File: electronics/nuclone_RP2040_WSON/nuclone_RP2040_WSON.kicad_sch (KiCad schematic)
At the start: 36 parts, among them J1 JTAG_2X05, J2 TYPE-C-31-M-12, J3 nuclone_small_left, J4 nuclone_small_right, SW1 RESET, SW2 Bootloader, U1 MCP1702-MB, U2 TPESD0504C6

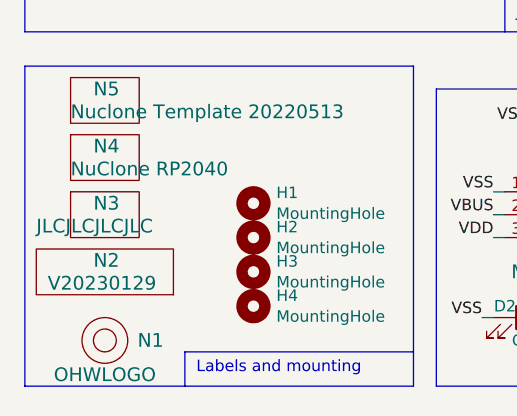
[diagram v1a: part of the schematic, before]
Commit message: updated 0402 and 0603 components, added crystal ground plane keepout
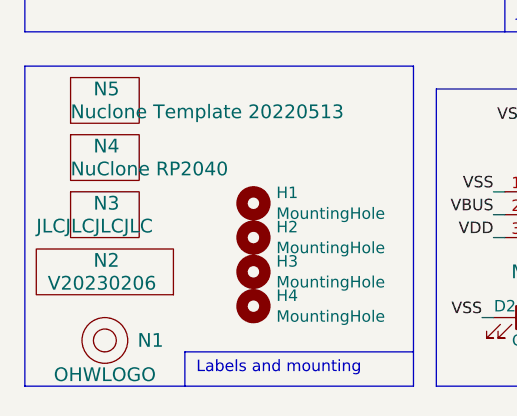
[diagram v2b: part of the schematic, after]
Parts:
- N2: value V20230129 -> V20230206
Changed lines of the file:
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@@
       (effects (font (size 1.524 1.524)) (justify left))
     )
-    (property "Value" "V20230129" (id 1) (at 17.78 182.88 0)
+    (property "Value" "V20230206" (id 1) (at 17.78 182.88 0)
       (effects (font (size 1.524 1.524)) (justify left))
     )
@@
     )
     (path "/00000000-0000-0000-0000-00005d6a68b9"
-      (reference "N2") (unit 1) (value "V20230129") (footprint "SquantorLabels:Label_Generic")
+      (reference "N2") (unit 1) (value "V20230206") (footprint "SquantorLabels:Label_Generic")
     )
     (path "/00000000-0000-0000-0000-00005d8b1b32"

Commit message: small updates
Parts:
- N2: value V20230206 -> V20230207
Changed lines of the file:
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@@
       (effects (font (size 1.524 1.524)) (justify left))
     )
-    (property "Value" "V20230206" (id 1) (at 17.78 182.88 0)
+    (property "Value" "V20230207" (id 1) (at 17.78 182.88 0)
       (effects (font (size 1.524 1.524)) (justify left))
     )
@@
     )
     (path "/00000000-0000-0000-0000-00005d6a68b9"
-      (reference "N2") (unit 1) (value "V20230206") (footprint "SquantorLabels:Label_Generic")
+      (reference "N2") (unit 1) (value "V20230207") (footprint "SquantorLabels:Label_Generic")
     )
     (path "/00000000-0000-0000-0000-00005d8b1b32"

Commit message: final check, updated versionnumber
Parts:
- N2: value V20230207 -> V20230211
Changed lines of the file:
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@@
       (effects (font (size 1.524 1.524)) (justify left))
     )
-    (property "Value" "V20230207" (id 1) (at 17.78 182.88 0)
+    (property "Value" "V20230211" (id 1) (at 17.78 182.88 0)
       (effects (font (size 1.524 1.524)) (justify left))
     )
@@
       (reference "#FLG01") (unit 1) (value "PWR_FLAG") (footprint "")
     )
+    (path "/00000000-0000-0000-0000-00006127a958/91ee7d48-3b1d-497b-89ca-6c620391c42e"
+      (reference "#FLG0101") (unit 1) (value "PWR_FLAG") (footprint "")
+    )
     (path "/00000000-0000-0000-0000-00005d820111"
       (reference "C1") (unit 1) (value "10u") (footprint "SquantorRcl:C_0603")
@@
     )
     (path "/00000000-0000-0000-0000-00005d6a68b9"
-      (reference "N2") (unit 1) (value "V20230207") (footprint "SquantorLabels:Label_Generic")
+      (reference "N2") (unit 1) (value "V20230211") (footprint "SquantorLabels:Label_Generic")
     )
     (path "/00000000-0000-0000-0000-00005d8b1b32"
